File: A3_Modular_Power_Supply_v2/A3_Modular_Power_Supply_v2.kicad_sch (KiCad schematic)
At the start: 70 parts, among them J1 JST-XH-S3B, J10 Conn_01x02_Pin, J11 Conn_01x02_Pin, J2 JST-XH-S3B, J3 JST-XH-S3B, J4 JST-XH-S3B, J5 JST-XH-S3B, J6 JST-XH-S3B, J7 JST-XH-S3B, Q1 CSD17522Q5A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

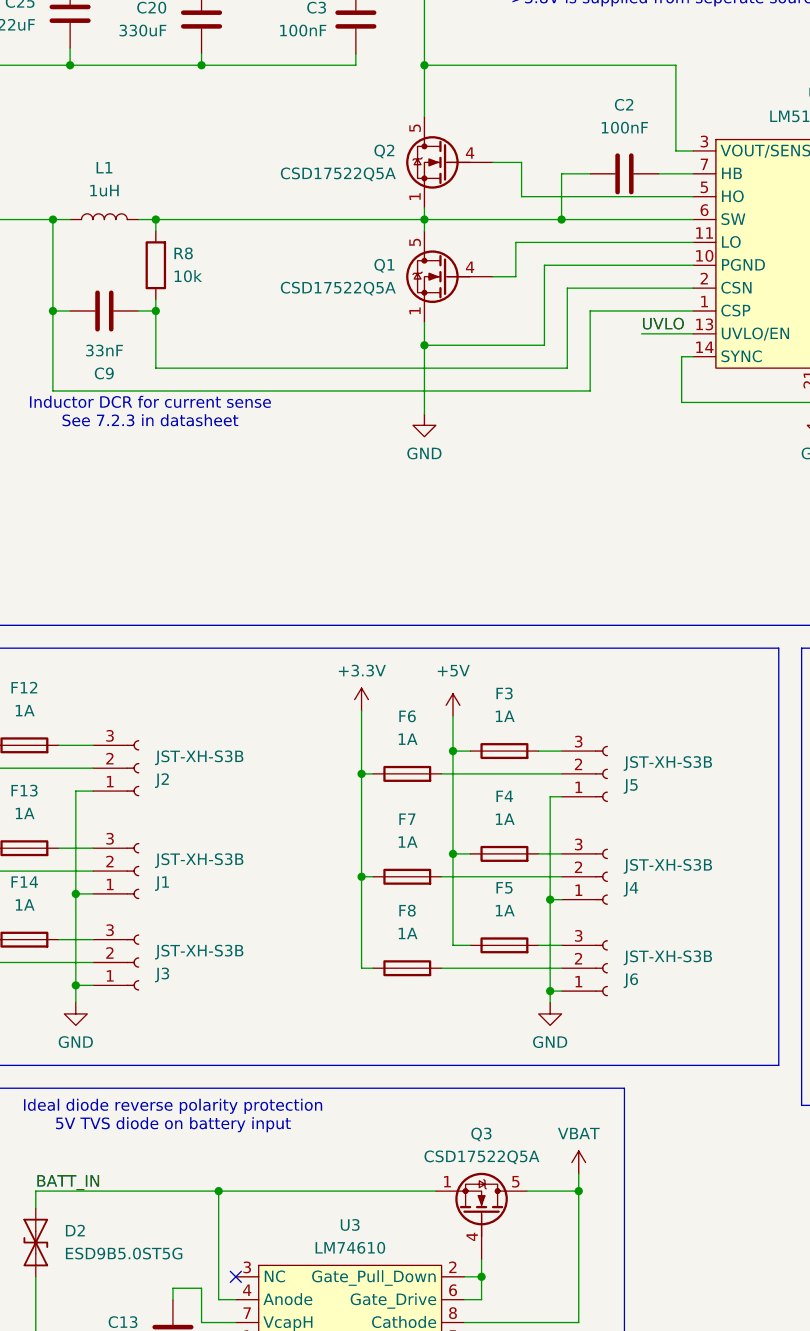
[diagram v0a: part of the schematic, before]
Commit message: Changed some capacitor package sizes
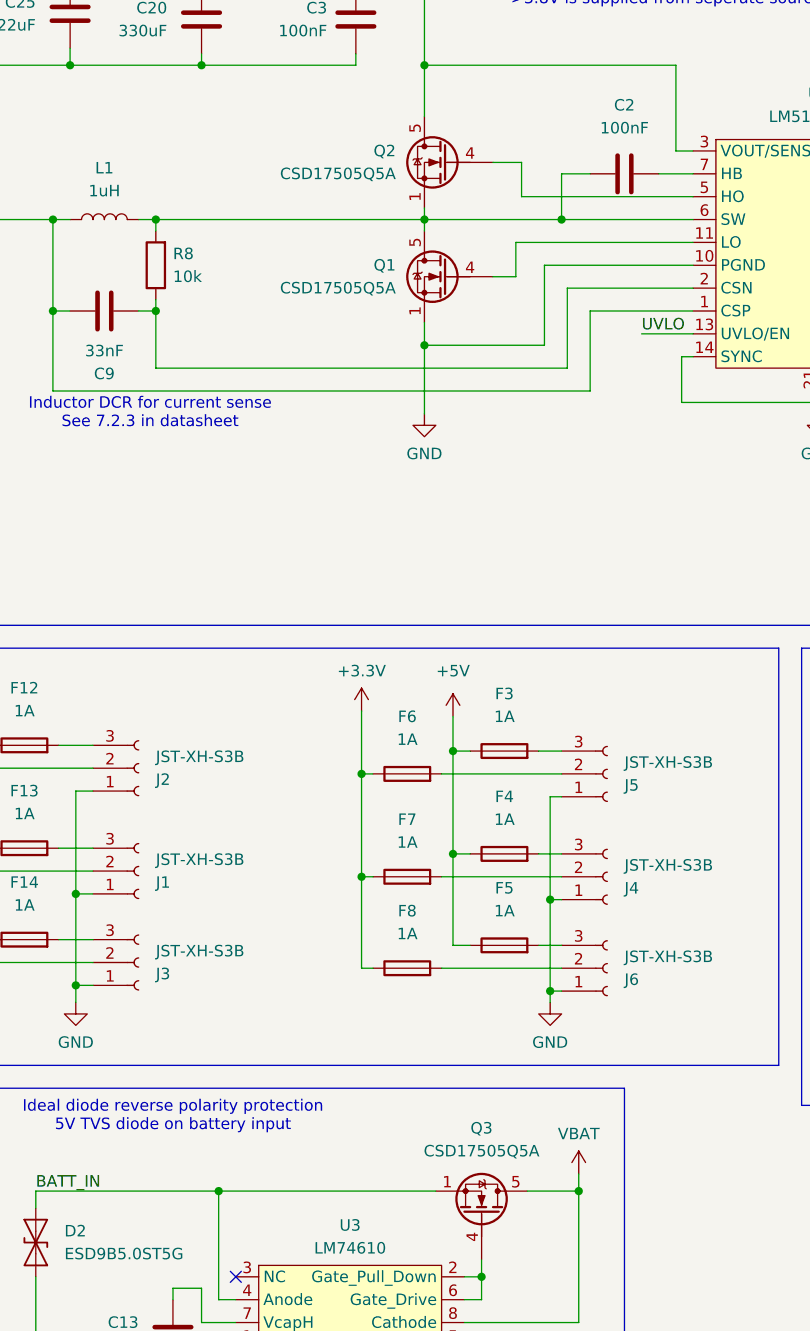
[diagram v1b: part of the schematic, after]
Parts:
- C15, C24, C4: footprint Capacitor_SMD:C_0402_1005Metric -> Capacitor_SMD:C_0603_1608Metric
- Q1, Q2, Q3: value CSD17522Q5A -> CSD17505Q5A
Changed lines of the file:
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@@
 			)
 		)
-		(property "Footprint" "Capacitor_SMD:C_0402_1005Metric"
+		(property "Footprint" "Capacitor_SMD:C_0603_1608Metric"
 			(at 271.4498 93.345 0)
 			(hide yes)
@@
 			)
 		)
-		(property "Footprint" "Capacitor_SMD:C_0402_1005Metric"
+		(property "Footprint" "Capacitor_SMD:C_0603_1608Metric"
 			(at 260.6548 86.995 0)
 			(hide yes)
@@
 			)
 		)
-		(property "Value" "CSD17522Q5A"
+		(property "Value" "CSD17505Q5A"
 			(at 132.08 69.2149 0)
 			(show_name no)
@@
 		(fields_autoplaced yes)
 		(property "Reference" "Q3"
-			(at 141.605 163.195 90)
+			(at 141.605 162.56 90)
 			(show_name no)
 			(do_not_autoplace no)
@@
 			)
 		)
-		(property "Value" "CSD17522Q5A"
-			(at 141.605 165.735 90)
+		(property "Value" "CSD17505Q5A"
+			(at 141.605 165.1 90)
 			(show_name no)
 			(do_not_autoplace no)
@@
 			)
 		)
-		(property "Value" "CSD17522Q5A"
+		(property "Value" "CSD17505Q5A"
 			(at 132.08 56.5149 0)
 			(show_name no)
@@
 			)
 		)
-		(property "Footprint" "Capacitor_SMD:C_0402_1005Metric"
+		(property "Footprint" "Capacitor_SMD:C_0603_1608Metric"
 			(at 195.2498 147.955 0)
 			(hide yes)
